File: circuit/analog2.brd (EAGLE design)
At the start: 100 x 80 mm, 66 parts, among them IC1 AD8532, IC2 74HC4052D, IC3 AD8532, IC4 74HC4066D

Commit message: - начали разводить плату
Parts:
- removed IC4: 74HC4066D, 40xx:SO14
- removed X3: (no value), con-phoenix-254:2POL254
- added C21: 1mk, rcl:C0603
- C3: device rcl:C0805 -> rcl:C1206
- C7: value 1mk -> 10mk; device rcl:C0603 -> rcl:C0805
- C8: value 47n -> 100n; device rcl:C0805 -> rcl:C0603
- IC1, IC3: value AD8532 -> OP07C; device linear:SO08 -> analog-devices:SO8
- R1: device rcl:R1206 -> rcl:R0805
- R18, R25: value 2.7k -> 5.6k
- R21: device rcl:R1206W -> rcl:R0805
- R6, R7: value 56k -> 10k
- R8: value 4.7 -> 22k
- moved C17 139.3 mm to (-54.6, 58.4)
- moved C19 122.3 mm to (-43.2, 58.4)
- moved C16 121.8 mm to (-36.8, 58.4)
- moved L3 108.1 mm to (-26.7, 53.3), turned to 0 degrees
- moved C14 101.2 mm to (-30.5, 58.4)
- moved C10 90.2 mm to (-17.8, 58.4)
- moved C20 86.7 mm to (-49.5, 58.4), turned to 0 degrees
- moved C18 81.4 mm to (3.81, 61.6)
- moved C11 64.1 mm to (-24.1, 58.4)
- moved C15 50.0 mm to (85.7, 26.7)
- moved R7 49.4 mm to (61.0, 64.1)
- moved L2 42.7 mm to (49.5, 73.7), turned to 0 degrees
- moved L4 42.4 mm to (50.8, 66.0)
- moved R6 41.9 mm to (63.5, 50.8)
- moved R8 35.9 mm to (61.0, 58.4)
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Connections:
- net V_IN- renamed N$30
- removed net GND: C5.2, C6.2
- removed net I_GAIN: IC4.12, X3.2
- removed net N$1: C4.2, IC1.1, IC1.2
- removed net N$30 (its old number): IC4.8, R18.2
- removed net N$31: IC4.11, R25.2
- removed net N$9: C20.2, IC3.3, R6.1, R7.2
- removed net V_GAIN: IC4.6, X3.1
- net +2.5V: now also C20.2, C7.1, IC3.3, R6.1, R7.2, R8.1; no longer C8.1, IC3.1, IC3.2, IC3.5, R5.1, R8.2
- net GNDA: now also C21.2, C5.2, C6.2, C7.2; no longer C7.1, IC4.13, IC4.5, IC4.7
- net N$10: now also C21.1, C8.1, R5.1, R8.2; no longer C7.2, R8.1
- net N$11: now also IC3.6; no longer IC3.7
- net N$2: now also C4.2; no longer IC1.3
- net N$21: now also R25.2; no longer IC4.10
- net N$23: now also R18.2; no longer IC4.9
- net N$5: now also IC1.2; no longer IC1.7
- net N$6: now also IC1.3; no longer IC1.5
- net N$7: now also IC1.7; no longer IC1.8
- net N$8: now also IC3.2; no longer IC3.6
- net VCC: now also IC3.7; no longer IC3.8, IC4.14
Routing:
- net N$32: track 32.9 -> 0.00 mm
- net GNDA: track 22.1 -> 54.4 mm
- net N$18: track 8.21 -> 25.0 mm
- net N$27: track 13.7 -> 0.00 mm
- net V_ADC: track 12.7 -> 0.00 mm
- net N$14: track 0.00 -> 11.9 mm
- net N$3: track 27.3 -> 16.8 mm
- net N$5: track 17.3 -> 7.13 mm
- net SPI_CS_V: track 10.1 -> 0.00 mm
- net SPI_SI: track 9.09 -> 0.00 mm
- net SPI_SCK: track 9.09 -> 0.00 mm
- net N$15: track 0.00 -> 8.30 mm
- net N$13: track 0.00 -> 7.56 mm
- net N$19: track 12.0 -> 5.21 mm
- net +5V: track 6.77 -> 0.00 mm
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
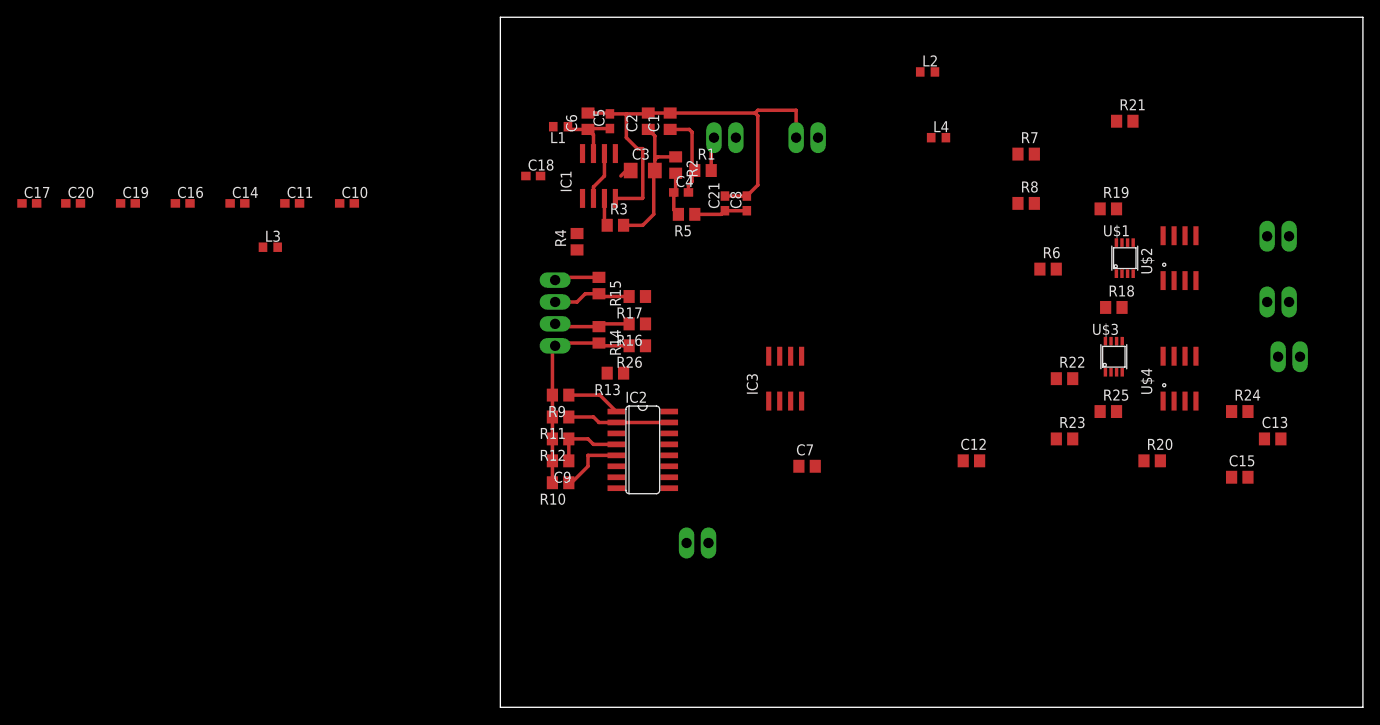
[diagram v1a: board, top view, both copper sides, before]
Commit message: - черновой вариант разводки, не проверяли как земля разведенна. Не добавляли пинов, чтобы осциллографом цепляться
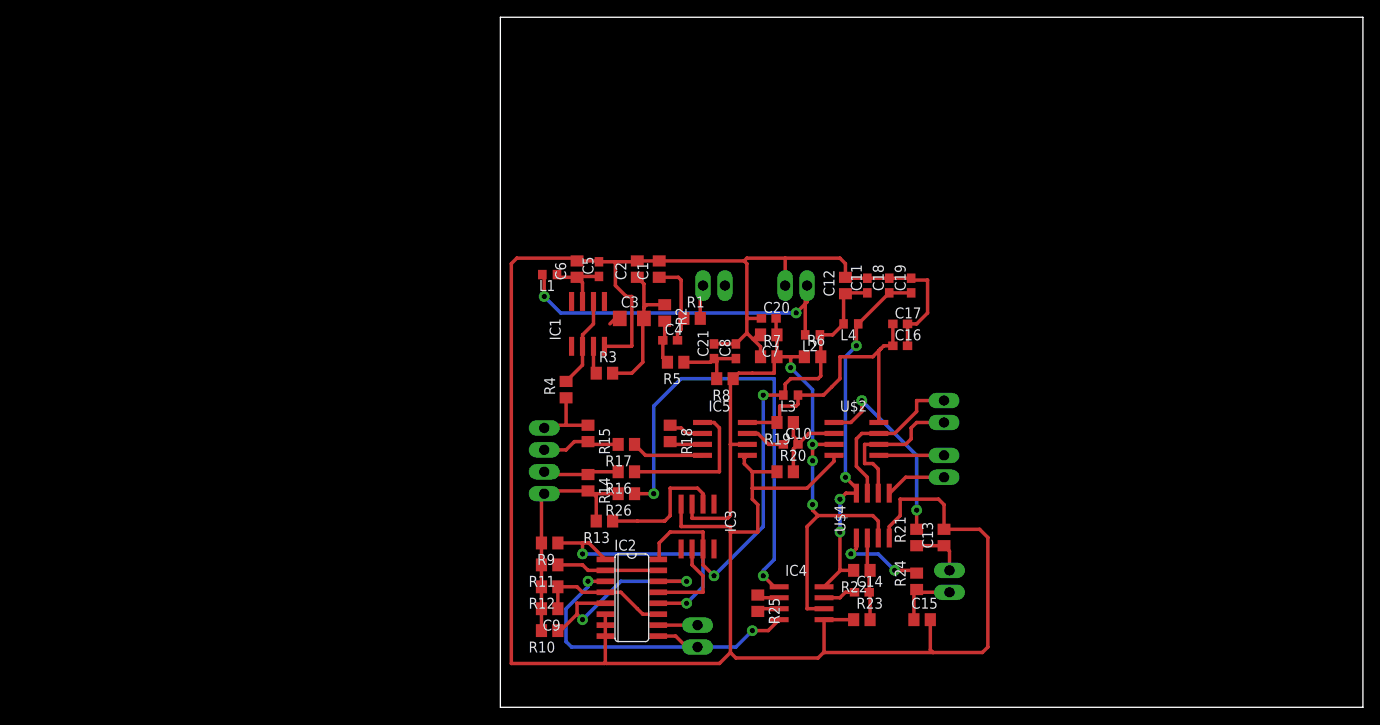
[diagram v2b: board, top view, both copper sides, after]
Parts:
- removed U$1, U$3: AD8221, balmer:SSOP08
- added IC4, IC5: AD8221R, balmer:SO8
- moved C17 101.9 mm to (46.4, 44.5)
- moved C19 91.3 mm to (47.6, 48.9), turned to 90 degrees
- moved C14 85.3 mm to (41.9, 13.3)
- moved C16 84.8 mm to (46.4, 41.9)
- moved C20 81.7 mm to (31.1, 45.1)
- moved C11 67.4 mm to (42.5, 48.9), turned to 90 degrees
- moved L3 62.7 mm to (33.7, 36.2), turned to 180 degrees
- moved C10 58.5 mm to (33.7, 30.5)
- moved R21 54.0 mm to (48.3, 19.7), turned to 90 degrees
- moved R18 53.5 mm to (19.7, 31.8), turned to 270 degrees
- moved X5 47.2 mm to (52.1, 14.6), turned to 270 degrees
- moved R25 46.3 mm to (29.8, 12.1), turned to 270 degrees
- moved R19 44.9 mm to (33.0, 33.0), turned to 180 degrees
- moved X6 43.7 mm to (51.4, 34.3), turned to 270 degrees
- moved C18 43.2 mm to (45.1, 48.9), turned to 90 degrees
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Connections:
- removed net I_IN+: R26.1, U$3.4
- removed net I_IN-: IC2.3, U$3.1
- new net N$1: IC5.4, R17.1
- new net N$9: IC4.3, R25.2
- net +2.5V: now also IC4.6, IC5.6
- net GNDA: now also IC4.5, IC5.5; no longer U$1.5, U$3.5
- net N$20: now also IC5.7; no longer U$1.7
- net N$21: now also IC4.2, R25.1; no longer R25.2, U$3.3
- net N$22: now also IC4.1, R26.1; no longer R25.1, U$3.2
- net N$23: now also IC5.3; no longer U$1.3
- net N$24: now also IC5.2; no longer U$1.2
- net N$29: now also IC4.7; no longer U$3.7
- net N$30: now also IC2.3, IC4.4; no longer R17.1, U$1.1
- net N$32: now also IC5.8; no longer U$1.8
- net N$34: now also IC4.8; no longer U$3.8
- net V_IN+: now also IC5.1; no longer U$1.4
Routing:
- net GNDA: track 54.4 -> 297.6 mm
- net +2.5V: track 0.00 -> 83.6 mm, vias 0 -> 4
- net VCC: track 0.00 -> 59.2 mm, vias 0 -> 2
- net N$22: track 0.00 -> 53.4 mm, vias 0 -> 2
- net N$34: track 0.00 -> 43.1 mm, vias 0 -> 4
- net +5V: track 0.00 -> 42.1 mm, vias 0 -> 2
- net N$30: track 0.00 -> 36.3 mm, vias 0 -> 2
- net N$32: track 0.00 -> 34.8 mm
- net N$12: track 6.29 -> 31.3 mm, vias 0 -> 2
- net N$28: track 0.00 -> 22.6 mm, vias 0 -> 2
- net SPI_SCK: track 0.00 -> 19.6 mm
- net N$13: track 7.56 -> 25.6 mm, vias 0 -> 2
- net SPI_SI: track 0.00 -> 17.9 mm
- net V_IN+: track 0.00 -> 17.2 mm
- net N$8: track 0.00 -> 15.4 mm
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
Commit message: - SO8
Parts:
- moved C11 3.18 mm to (42.5, 45.7)
- moved C12 3.18 mm to (40.0, 45.7)
- moved C17 3.18 mm to (46.4, 41.3)
- moved C18 3.18 mm to (45.1, 45.7)
- moved C19 3.18 mm to (47.6, 45.7)
- moved C20 3.18 mm to (31.1, 41.9)
- moved C3 3.18 mm to (15.2, 41.9)
- moved C4 3.18 mm to (19.7, 39.4)
- moved IC1 3.18 mm to (10.2, 41.3)
- moved L4 3.18 mm to (40.6, 41.3)
- moved R1 3.18 mm to (22.2, 41.9)
- moved R19 3.18 mm to (33.0, 29.8)
- moved R5 3.18 mm to (20.3, 36.8)
- moved R8 3.18 mm to (26.0, 34.9)
- moved X2 3.18 mm to (34.3, 45.7)
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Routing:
- net GNDA: track 297.6 -> 294.6 mm
- net SPI_SI: track 17.9 -> 17.1 mm
- net SPI_SCK: track 19.6 -> 18.8 mm
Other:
- board size 100 x 80 mm -> 56.2 x 50.8 mm

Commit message: - пины для теста
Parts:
- added LSP1, LSP2: LSP10, solpad:LSP10
- added X3, X9: 332-02, con-garry:332-02
- moved R23 1.91 mm to (41.9, 5.08)
- moved R20 1.27 mm to (33.0, 22.9)
- moved R18 0.63 mm to (19.1, 28.6)
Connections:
- net N$1: now also X3.2
- net N$20: now also LSP1.MP
- net N$22: now also X9.1
- net N$29: now also LSP2.MP
- net N$30: now also X9.2
- net V_IN+: now also X3.1
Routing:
- net N$22: track 53.4 -> 57.4 mm
- net N$29: track 3.80 -> 6.68 mm
- net N$25: track 9.68 -> 12.5 mm
- net N$30: track 36.3 -> 39.0 mm
- net N$20: track 4.70 -> 6.78 mm
- net V_IN+: track 17.2 -> 18.9 mm
- net N$27: track 10.9 -> 12.1 mm
- net N$24: track 4.14 -> 4.70 mm
- net N$23: track 3.88 -> 4.44 mm

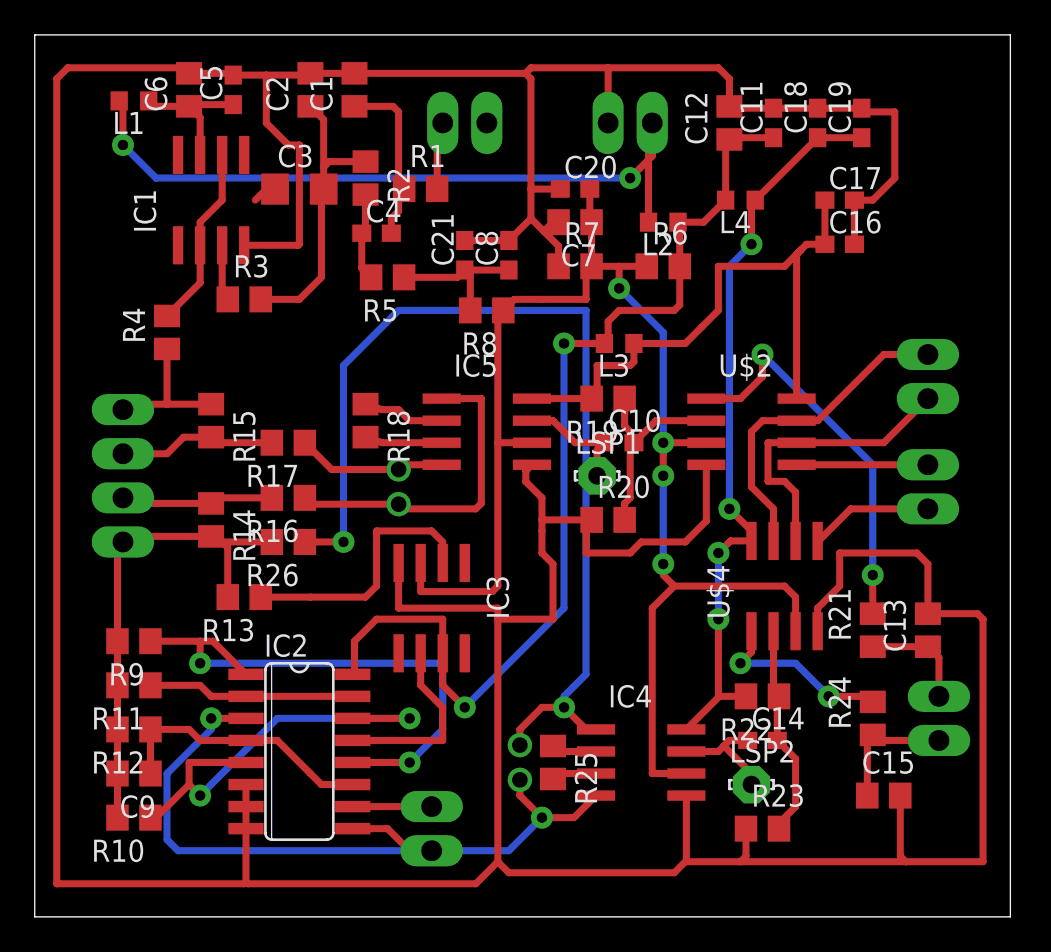
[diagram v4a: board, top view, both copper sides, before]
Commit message: - исходный код скопипастили для F103 демоплатки
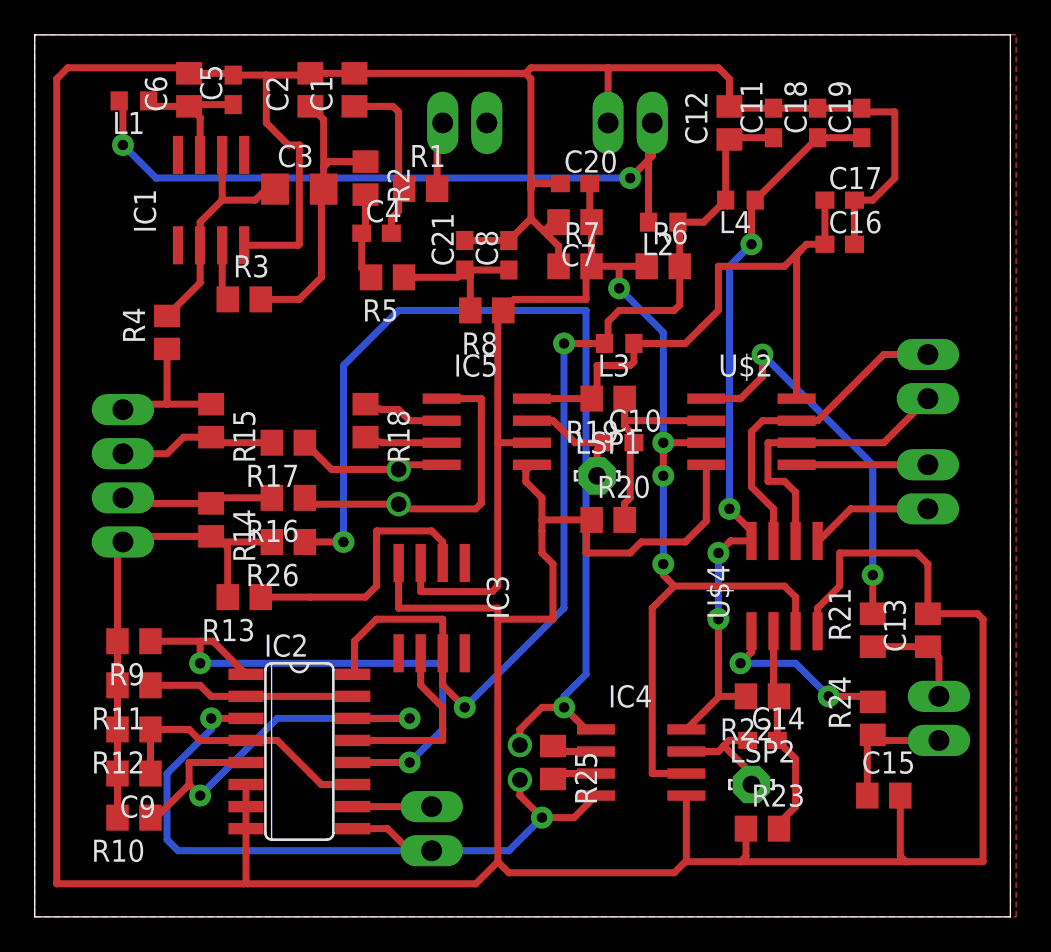
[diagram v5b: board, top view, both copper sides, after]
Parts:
- moved C20 0.32 mm to (31.1, 42.2)
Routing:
- net N$5: track 12.0 -> 13.9 mm
- added copper zone on layer 1, net GNDA
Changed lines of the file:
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@@
 <layer number="27" name="tValues" color="7" fill="1" visible="yes" active="yes"/>
 <layer number="28" name="bValues" color="7" fill="1" visible="yes" active="yes"/>
-<layer number="29" name="tStop" color="7" fill="3" visible="no" active="yes"/>
-<layer number="30" name="bStop" color="7" fill="6" visible="no" active="yes"/>
-<layer number="31" name="tCream" color="7" fill="4" visible="no" active="yes"/>
-<layer number="32" name="bCream" color="7" fill="5" visible="no" active="yes"/>
-<layer number="33" name="tFinish" color="6" fill="3" visible="no" active="yes"/>
-<layer number="34" name="bFinish" color="6" fill="6" visible="no" active="yes"/>
-<layer number="35" name="tGlue" color="7" fill="4" visible="no" active="yes"/>
-<layer number="36" name="bGlue" color="7" fill="5" visible="no" active="yes"/>
-<layer number="37" name="tTest" color="7" fill="1" visible="no" active="yes"/>
-<layer number="38" name="bTest" color="7" fill="1" visible="no" active="yes"/>
+<layer number="29" name="tStop" color="7" fill="3" visible="yes" active="yes"/>
+<layer number="30" name="bStop" color="7" fill="6" visible="yes" active="yes"/>
+<layer number="31" name="tCream" color="7" fill="4" visible="yes" active="yes"/>
+<layer number="32" name="bCream" color="7" fill="5" visible="yes" active="yes"/>
+<layer number="33" name="tFinish" color="6" fill="3" visible="yes" active="yes"/>
+<layer number="34" name="bFinish" color="6" fill="6" visible="yes" active="yes"/>
+<layer number="35" name="tGlue" color="7" fill="4" visible="yes" active="yes"/>
+<layer number="36" name="bGlue" color="7" fill="5" visible="yes" active="yes"/>
+<layer number="37" name="tTest" color="7" fill="1" visible="yes" active="yes"/>
+<layer number="38" name="bTest" color="7" fill="1" visible="yes" active="yes"/>
 <layer number="39" name="tKeepout" color="4" fill="11" visible="yes" active="yes"/>
 <layer number="40" name="bKeepout" color="1" fill="11" visible="yes" active="yes"/>
@@
 <layer number="42" name="bRestrict" color="1" fill="10" visible="yes" active="yes"/>
 <layer number="43" name="vRestrict" color="2" fill="10" visible="yes" active="yes"/>
-<layer number="44" name="Drills" color="7" fill="1" visible="no" active="yes"/>
-<layer number="45" name="Holes" color="7" fill="1" visible="no" active="yes"/>
-<layer number="46" name="Milling" color="3" fill="1" visible="no" active="yes"/>
-<layer number="47" name="Measures" color="7" fill="1" visible="no" active="yes"/>
+<layer number="44" name="Drills" color="7" fill="1" visible="yes" active="yes"/>
+<layer number="45" name="Holes" color="7" fill="1" visible="yes" active="yes"/>
+<layer number="46" name="Milling" color="3" fill="1" visible="yes" active="yes"/>
+<layer number="47" name="Measures" color="7" fill="1" visible="yes" active="yes"/>
 <layer number="48" name="Document" color="7" fill="1" visible="yes" active="yes"/>
 <layer number="49" name="Reference" color="7" fill="1" visible="yes" active="yes"/>
@@
 <attribute name="OC_FARNELL" value="unknown" x="53.975" y="92.71" size="1.778" layer="28" rot="MR180" display="off"/>
 </element>
-<element name="C20" library="rcl" package="C0603" value="100n" x="31.115" y="41.91"/>
+<element name="C20" library="rcl" package="C0603" value="100n" x="31.115" y="42.2275"/>
 <element name="IC1" library="analog-devices" package="SO8" value="OP07C" x="10.16" y="41.275">
 <attribute name="OC_NEWARK" value="88H0179" x="27.94" y="26.035" size="1.778" layer="27" display="off"/>
@@
 <wire x1="9.525" y1="40.005" x2="10.795" y2="41.275" width="0.4064" layer="1"/>
 <wire x1="10.795" y1="41.275" x2="10.795" y2="43.875" width="0.4064" layer="1"/>
-<wire x1="11.115" y1="41.595" x2="10.795" y2="41.275" width="0" layer="19" extent="1-16"/>
 <wire x1="13.84" y1="41.91" x2="13.335" y2="41.91" width="0.4064" layer="1"/>
 <wire x1="13.335" y1="41.91" x2="12.7" y2="41.275" width="0.4064" layer="1"/>
-<wire x1="12.7" y1="41.275" x2="10.795" y2="41.275" width="0" layer="19" extent="1-16"/>
 <wire x1="9.525" y1="38.675" x2="9.525" y2="36.51" width="0.4064" layer="1"/>
 <wire x1="9.525" y1="36.51" x2="7.62" y2="34.605" width="0.4064" layer="1"/>
+<wire x1="12.7" y1="41.275" x2="10.795" y2="41.275" width="0.4064" layer="1"/>
 </signal>
 <signal name="GENERATOR">
@@
 <wire x1="31.75" y1="37.15" x2="32.065" y2="37.465" width="0.4064" layer="1"/>
 <wire x1="32.065" y1="40.005" x2="32.065" y2="37.465" width="0.4064" layer="1"/>
-<wire x1="31.965" y1="41.91" x2="31.965" y2="40.105" width="0.4064" layer="1"/>
+<wire x1="31.965" y1="42.2275" x2="31.965" y2="40.105" width="0.4064" layer="1"/>
 <wire x1="31.965" y1="40.105" x2="32.065" y2="40.005" width="0.4064" layer="1"/>
 <wire x1="31.75" y1="35.56" x2="29.21" y2="35.56" width="0.4064" layer="1"/>
@@
 <wire x1="30.165" y1="40.005" x2="29.845" y2="40.005" width="0.4064" layer="1"/>
 <wire x1="29.845" y1="40.005" x2="29.3175" y2="39.4775" width="0.4064" layer="1"/>
-<wire x1="30.265" y1="41.91" x2="28.575" y2="41.91" width="0.4064" layer="1"/>
 <wire x1="12.1666" y1="5.08" x2="12.1666" y2="2.0066" width="0.4064" layer="1"/>
 <wire x1="12.1666" y1="2.0066" x2="12.065" y2="1.905" width="0.4064" layer="1"/>
@@
 <wire x1="31.75" y1="20.955" x2="31.75" y2="22.54" width="0.4064" layer="1"/>
 <wire x1="31.75" y1="22.54" x2="32.07" y2="22.86" width="0.4064" layer="1"/>
+<wire x1="30.265" y1="42.2275" x2="28.575" y2="42.2275" width="0.4064" layer="1"/>
+<wire x1="28.575" y1="42.2275" x2="28.575" y2="41.91" width="0.4064" layer="1"/>
+<polygon width="0.4064" layer="1" pour="hatch" isolate="0.6096">
+<vertex x="0" y="0"/>
+<vertex x="56.515" y="0"/>
+<vertex x="56.515" y="50.8"/>
+<vertex x="0" y="50.8"/>
+</polygon>
 </signal>
 <signal name="VCC">
@@
 <contactref element="R20" pad="2"/>
 <contactref element="U$2" pad="2"/>
-<wire x1="33.97" y1="29.845" x2="33.97" y2="28.26" width="0.4064" layer="1"/>
+<wire x1="33.97" y1="29.845" x2="33.97" y2="28.575" width="0.4064" layer="1"/>
+<wire x1="33.97" y1="28.575" x2="33.97" y2="28.26" width="0.4064" layer="1"/>
 <wire x1="33.97" y1="28.26" x2="34.29" y2="27.94" width="0.4064" layer="1"/>
 <wire x1="34.29" y1="27.94" x2="34.29" y2="27.52" width="0.4064" layer="1"/>
 <wire x1="34.29" y1="27.52" x2="34.505" y2="27.305" width="0.4064" layer="1"/>
 <wire x1="38.675" y1="28.575" x2="35.775" y2="28.575" width="0.4064" layer="1"/>
-<wire x1="35.775" y1="28.575" x2="34.505" y2="27.305" width="0.4064" layer="1"/>
 <wire x1="33.97" y1="22.86" x2="33.97" y2="23.81" width="0.4064" layer="1"/>
 <wire x1="33.97" y1="23.81" x2="34.29" y2="24.13" width="0.4064" layer="1"/>
 <wire x1="34.29" y1="24.13" x2="34.29" y2="27.09" width="0.4064" layer="1"/>
 <wire x1="34.29" y1="27.09" x2="34.505" y2="27.305" width="0.4064" layer="1"/>
+<wire x1="35.775" y1="28.575" x2="33.97" y2="28.575" width="0.4064" layer="1"/>
 </signal>
 <signal name="N$28">
